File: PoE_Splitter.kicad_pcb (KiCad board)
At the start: 2 copper layers, 104 x 62 mm, 120 parts, among them J1 R-RJ45R10P-B000, J2 R-RJ45R10P-B000, J3 AMASS_XT30PW-M, J4 AMASS_XT30PW-M, J5 AMASS_XT30PW-M, Q1 BSS127S, U1 VCF4812EBO-120WR3-N, U2 TPS2372, U3 MPQ8875A, U4 PD70224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

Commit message: add desc text
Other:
- board text added: "acha666/PoE_Splitter ${BRANCH}-${SHORT_SHA}"

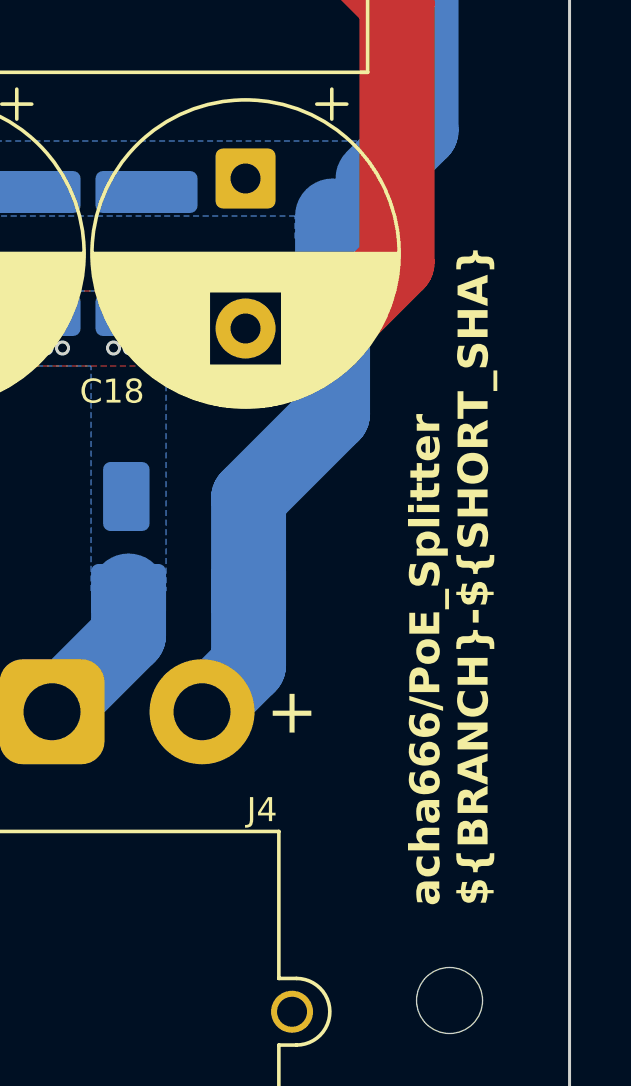
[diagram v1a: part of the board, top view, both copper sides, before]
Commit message: add sheet titles
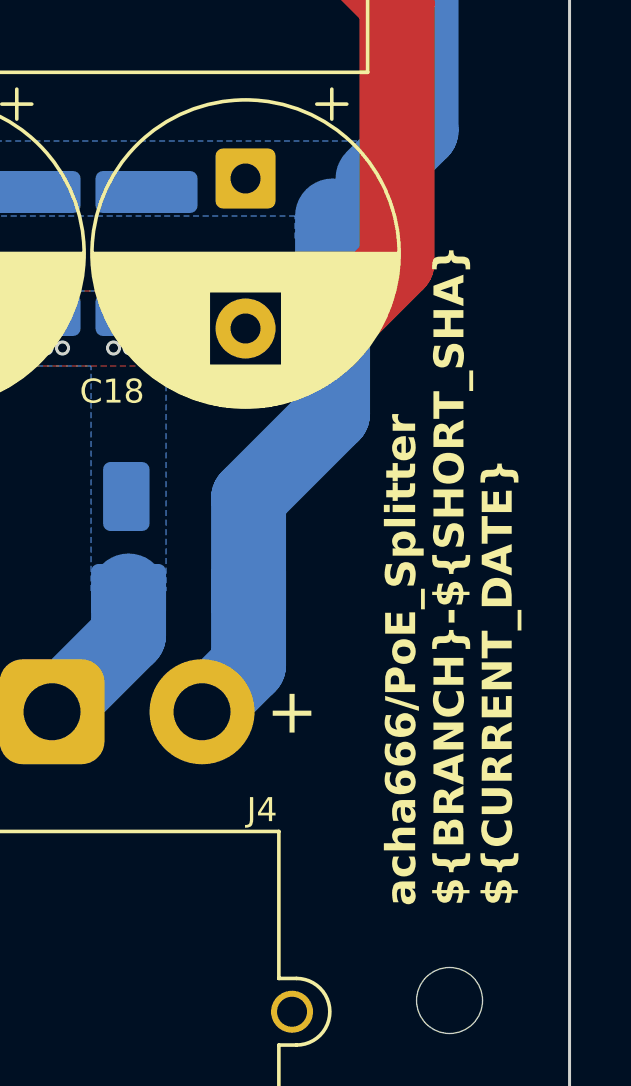
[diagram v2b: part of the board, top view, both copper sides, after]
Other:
- board text added: "acha666/PoE_Splitter ${BRANCH}-${SHORT_SHA} ${CURRENT_DATE}"
- board text removed: "acha666/PoE_Splitter ${BRANCH}-${SHORT_SHA}"
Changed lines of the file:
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@@
 	)
 	(paper "A4")
+	(title_block
+		(title "PoE_Splitter")
+		(date "${CURRENT_DATE}")
+		(rev "${SHORT_SHA}")
+		(company "Acha")
+		(comment 1 "GPL-3.0 Licensed")
+		(comment 2 "https://github.com/acha666/PoE_Splitter@${BRANCH}")
+	)
 	(layers
 		(0 "F.Cu" signal)
@@
 			(at 0 -1.43 90)
 			(layer "B.Fab")
+			(hide yes)
 			(effects
 				(font
@@
 			(at 0 -1.43 0)
 			(layer "B.Fab")
+			(hide yes)
 			(effects
 				(font
@@
 			(at 0 -1.43 0)
 			(layer "B.Fab")
+			(hide yes)
 			(effects
 				(font
@@
 			(at 0 -1.75 0)
 			(layer "B.Fab")
+			(hide yes)
 			(effects
 				(font
@@
 			(at 0 -1.43 0)
 			(layer "B.Fab")
+			(hide yes)
 			(effects
 				(font
@@
 		(layer "Edge.Cuts")
 	)
-	(gr_text "acha666/PoE_Splitter\n${BRANCH}-${SHORT_SHA}"
+	(gr_text "acha666/PoE_Splitter\n${BRANCH}-${SHORT_SHA}\n${CURRENT_DATE}"
 		(at 196.5 118.85 90)
 		(layer "F.SilkS")
@@
 		(layer "B.Cu")
 		(hatch none 0.1)
-		(priority 30023)
+		(priority 30024)
 		(attr
 			(teardrop
@@
 		(polygon
 			(pts
-				(xy 116.025 72.875) (xy 116.006258 72.997033) (xy 115.940388 73.168129) (xy 115.91655 73.222049)
-				(xy 115.840224 73.398463) (xy 116.225 73.751) (xy 116.609776 73.398463) (xy 116.53345 73.222049)
-				(xy 116.454692 73.031765) (xy 116.432745 72.951828) (xy 116.425 72.875)
+				(xy 116.425 74.625) (xy 116.443742 74.502967) (xy 116.509612 74.331871) (xy 116.53345 74.277951)
+				(xy 116.609776 74.101537) (xy 116.225 73.749) (xy 115.840224 74.101537) (xy 115.91655 74.277951)
+				(xy 115.995308 74.468235) (xy 116.017255 74.548172) (xy 116.025 74.625)
 			)
 		)
@@
 		(layer "B.Cu")
 		(hatch none 0.1)
-		(priority 30024)
+		(priority 30023)
 		(attr
 			(teardrop
@@
 		(polygon
 			(pts
-				(xy 116.425 74.625) (xy 116.443742 74.502967) (xy 116.509612 74.331871) (xy 116.53345 74.277951)
-				(xy 116.609776 74.101537) (xy 116.225 73.749) (xy 115.840224 74.101537) (xy 115.91655 74.277951)
-				(xy 115.995308 74.468235) (xy 116.017255 74.548172) (xy 116.025 74.625)
+				(xy 116.025 72.875) (xy 116.006258 72.997033) (xy 115.940388 73.168129) (xy 115.91655 73.222049)
+				(xy 115.840224 73.398463) (xy 116.225 73.751) (xy 116.609776 73.398463) (xy 116.53345 73.222049)
+				(xy 116.454692 73.031765) (xy 116.432745 72.951828) (xy 116.425 72.875)
 			)
 		)
@@
 		(layer "B.Cu")
 		(hatch none 0.1)
-		(priority 30026)
+		(priority 30025)
 		(attr
 			(teardrop
@@
 		(layer "B.Cu")
 		(hatch none 0.1)
-		(priority 30025)
+		(priority 30026)
 		(attr
 			(teardrop

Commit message: MPQ boost cap value MPQ PG pull-up res all res value unit naming
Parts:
- C21, C23: value 10nF -> 100nF
- R1: value 24.9K -> 24.9kΩ
- R10: value 90.9R -> 90.9Ω
- R11: value 49.9K -> 49.9kΩ
- R12: value 220K -> 220kΩ
- R13, R17, R2: value 0R -> 0Ω
- R14: value 1.3K -> 1.3kΩ
- R16: value 33K -> 33kΩ
- R21, R22, R23, R24, R25, R26, R27, R29: value 75R -> 75Ω
- R30: value 110kΩ -> 10kΩ
- R31, R32: value 10kΩ -> 5.1kΩ
- R9: value 63.4R -> 63.4Ω
